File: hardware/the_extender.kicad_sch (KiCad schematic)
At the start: 115 parts, among them J0 TYPE-C 24P QT 143, J1 TYPE-C-31-M-16, J2 U231-091N-3BLRC11, J3 PJ-327D-5A, J4 PJ-327D-5A, J5 AF 10.0 HC6.3, Q6 SSM3J332R,LF, U1 IP5306-I2C, U2 RP2040, U3 W25Q32JVSS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

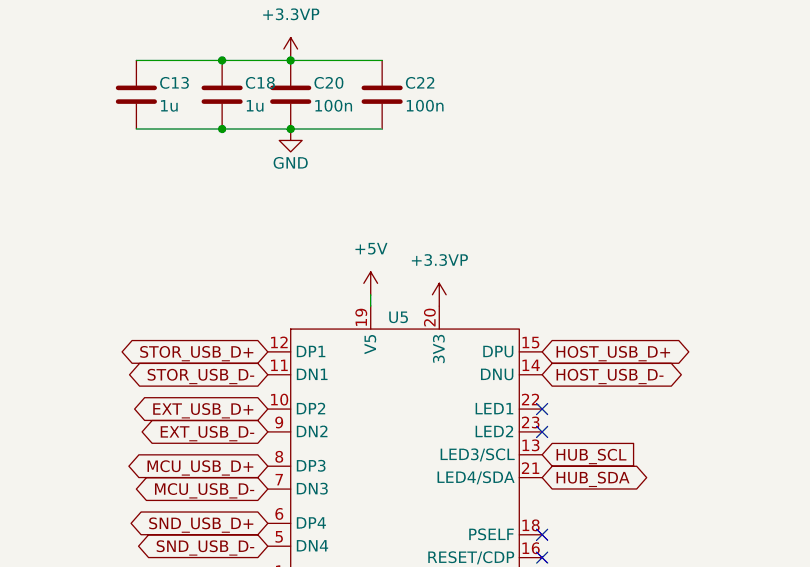
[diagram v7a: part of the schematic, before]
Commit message: update LCSC parts
i always forgot to update the schematic :facepalm:
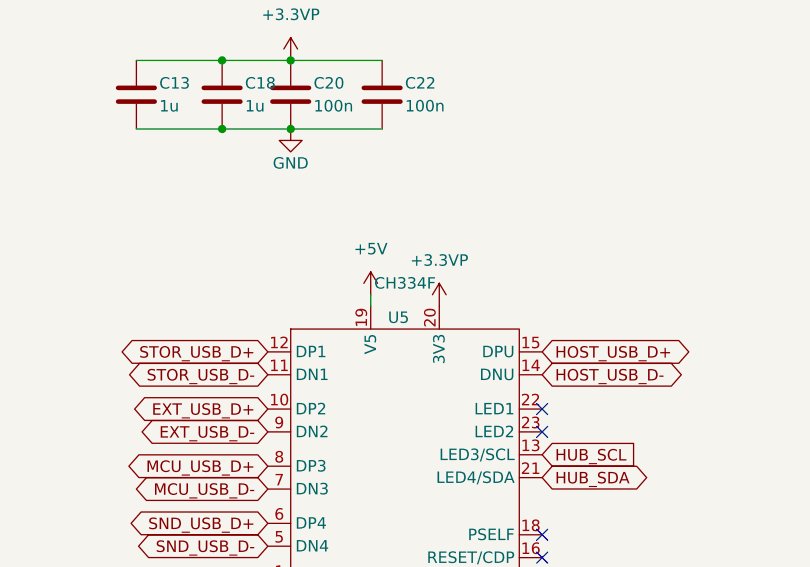
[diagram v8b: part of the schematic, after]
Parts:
- U5: value ~ -> CH334F
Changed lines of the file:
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@@
       (effects (font (size 1.27 1.27)) (justify left))
     )
-    (property "Value" "~" (at 212.09 47.625 0)
+    (property "Value" "CH334F" (at 212.09 47.625 0)
       (effects (font (size 1.27 1.27)))
     )
